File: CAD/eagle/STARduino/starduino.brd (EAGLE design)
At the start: 160 x 100 mm, 129 parts, among them J1 MICRO_SD, J2 J30J-9, J3 J30J-15, J4 J30J-31, J5 RPI-ZERO, J6 RPI-CSI, Q1 FDG8842CZ, Q2 FDG8842CZ, Q3 FDG8842CZ, Q4 FDG8842CZ, Q5 DMMT5401, Q6 DMG2305UX, T1 750313972, U1 ATSAMD21G18, U10 TCA9535_RTW_24, U11 DRV8846RGER, U12 MC14504BDTG, U13 PCA9306DCT, U14 MC74VHC1GT125DT, U15 MC74VHC1GT125DT, U16 MIC5216, U17 LT8301, U2 P82B715, U3 ADXL375BCCZ, U4 MAX31725MTA+, U5 LTC3112FE, U6 DS3231MZ+, U7 BMX055, U8 MT25QL01GBBB8ESF-0AAT, U9 LT3465/A

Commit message: more layout things, MDM adjustments
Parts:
- C1, C2: value 100nF -> 10uF; device resistor:C0603 -> resistor:C1206
- C10, C24, C25: value 1uF -> 100nF
- C11: value 10uF -> 22pF
- C12, C17: value 10uF -> 47pF
- C14: value 100nF -> 680pF
- C15, C3, C4: value 100nF -> 1uF
- C16: value 100nF -> 4.7uF; device resistor:C0603 -> CM_passives:KEMET_B
- C18: value 100nF -> 47uF; device resistor:C0603 -> resistor:C1210
- C19: value 100nF -> 10uF
- C20: value 1nF -> 10uF
- C26: value 10uF -> 1uF; device rcl:C0603 -> resistor:C0603
- C27: value 100nF -> 1uF; device rcl:C0603 -> resistor:C0603
- C28: value 2.2uF -> 1μF; device rcl:C0603 -> resistor:C0603
- C29: value 100nF -> 4.7uF; device resistor:C0603 -> resistor:A/3216-18R
- C30: value 1uF -> 10uF
- C31: value 10uF -> 100nF; device resistor:C1206 -> resistor:C0603
- C32: value 680pF -> 100nF
- C33: value 22pF -> 100nF
- C34, C35: value 47pF -> 100nF
- C36: value 47uF -> 100nF; device resistor:C1210 -> resistor:C0603
- C37: value 1uF -> 2.2uF; device resistor:C0603 -> rcl:C0603
- C38: value 4.7uF -> 10uF; device resistor:A/3216-18R -> rcl:C0603
- C39: value 10uF -> 100nF; device resistor:C1206 -> rcl:C0603
- C40: value 4.7uF -> 1uF; device CM_passives:KEMET_B -> resistor:C0603
- C41: value 1μF -> 100nF
- C5: value 1uF -> 1nF
- C6: value 6.8pF -> 100nF
- C8: value 100nF -> 6.8pF
- D1: value CMHD4448 -> CMDZ5257B; device CM_diodes:SOD123 -> CM_diodes:SOD323-W
- D2: value CMDZ5257B -> CMHD4448; device CM_diodes:SOD323-W -> CM_diodes:SOD123
- J1: value MICRO_SD -> J30J-9; device NR_connectors:MICROSD_PUSH_PUSH_AMPHENOL -> CM_J30J:ZKN-9
- J2: value J30J-9 -> MICRO_SD; device CM_J30J:ZKN-9 -> NR_connectors:MICROSD_PUSH_PUSH_AMPHENOL
- L1: value 10uH -> 22uH; device AR_passives:0603 -> AR_passives:VLF504012MT(TDK)
- L2: value 10uH -> 4.7uH; device AR_passives:0603 -> CM_passives:SRP5030
- L5: value 4.7uH -> 10uH; device CM_passives:SRP5030 -> AR_passives:0603
- L6: value 22uH -> 10uH; device AR_passives:VLF504012MT(TDK) -> AR_passives:0603
- Q3: value FDG8842CZ -> DMMT5401; device NR_Transistor:SC-70-6 -> transistor-pnp:SOT-26
- Q4: value FDG8842CZ -> DMG2305UX; device NR_Transistor:SC-70-6 -> microbuilder:SOT23-R
- Q5: value DMMT5401 -> FDG8842CZ; device transistor-pnp:SOT-26 -> NR_Transistor:SC-70-6
- Q6: value DMG2305UX -> FDG8842CZ; device microbuilder:SOT23-R -> NR_Transistor:SC-70-6
- R10: value 1.05 -> 100k; device rcl:R0603 -> resistor:R0603
- R11, R14: value 10k -> 191k; device rcl:R0603 -> resistor:R0603
- R12: value 10k -> 100k; device rcl:R0603 -> resistor:R0603
- R13: value 10k -> 4.7k; device rcl:R0603 -> resistor:R0603
- R15: value 4.7k -> 10k; device rcl:R0603 -> resistor:R0603
- R16: value 4.7k -> 47k; device rcl:R0603 -> resistor:R0603
- R17: value 220k -> 10k
- R18: value 10k -> 3.6k; device rcl:R0603 -> resistor:R0603
- R19: value 4.7k -> 6.8k
- R22: value 100k -> 10k; device resistor:R0603 -> rcl:R0603
- R23: value 191k -> 10k; device resistor:R0603 -> rcl:R0603
- R24: value 100k -> 1.05; device resistor:R0603 -> rcl:R0603
- R25: value 191k -> 1.05; device resistor:R0603 -> rcl:R0603
- R26: value 191k -> 100k
- R27: value 100k -> 4.7k
- R29: value 100k -> 4.7k; device resistor:R0603 -> rcl:R0603
- R3: value 3.6k -> 270k
- R30: value 33k -> 220k; device resistor:R0603 -> rcl:R0603
- R31: value 33k -> 10k; device resistor:R0603 -> rcl:R0603
- R32: value 158k -> 4.7k; device resistor:R0603 -> rcl:R0603
- R33: value 845k -> 4.7k
- R34: device resistor:R0603 -> rcl:R0603
- R35: value 270k -> 100k
- R36: value 47k -> 4.7k
- R37: value 10k -> 191k
- R4: value 6.8k -> 6.2
- R5, R6: value 4.7k -> 33k
- R7: value 4.7k -> 845k
- R8: value 6.2 -> 158k
- R9: value 1.05 -> 10k; device rcl:R0603 -> resistor:R0603
- U1: value ATSAMD21G18 -> LT8301; device AR_mcu:48-TQFP -> CM_IC:SOT23-5L
- U10: value TCA9535_RTW_24 -> MC74VHC1GT125DT; device MotorDriver:RTW24_2P45X2P45 -> MotorDriver:TSOP-5
- U11: value DRV8846RGER -> TCA9535_RTW_24; device MotorDriver:VQFN6 -> MotorDriver:RTW24_2P45X2P45
- U12: value MC14504BDTG -> MAX31725MTA+; device MotorDriver:TSSOP16 -> NR_IC:DFN-8
- U13: value PCA9306DCT -> BMX055; device MotorDriver:SSOP8 -> NR_IC:LGA-20
- U14: value MC74VHC1GT125DT -> DRV8846RGER; device MotorDriver:TSOP-5 -> MotorDriver:VQFN6
- U15: value MC74VHC1GT125DT -> P82B715; device MotorDriver:TSOP-5 -> CM_IC:SO8
- U16: value MIC5216 -> MC74VHC1GT125DT; device CM_IC:SOT23-5L -> MotorDriver:TSOP-5
- U17: value LT8301 -> PCA9306DCT; device CM_IC:SOT23-5L -> MotorDriver:SSOP8
- U2: value P82B715 -> LT3465/A; device CM_IC:SO8 -> AR_IC:SOT23-6
- U3: value ADXL375BCCZ -> LTC3112FE; device NR_IC:LGA-14 -> CM_IC:TSSOP20
- U4: value MAX31725MTA+ -> DS3231MZ+; device NR_IC:DFN-8 -> NR_IC:SOIC-8
- U5: value LTC3112FE -> MT25QL01GBBB8ESF-0AAT; device CM_IC:TSSOP20 -> NR_IC:SOP2-16
- U6: value DS3231MZ+ -> ATSAMD21G18; device NR_IC:SOIC-8 -> AR_mcu:48-TQFP
- U7: value BMX055 -> MIC5216; device NR_IC:LGA-20 -> CM_IC:SOT23-5L
- U8: value MT25QL01GBBB8ESF-0AAT -> ADXL375BCCZ; device NR_IC:SOP2-16 -> NR_IC:LGA-14
- U9: value LT3465/A -> MC14504BDTG; device AR_IC:SOT23-6 -> MotorDriver:TSSOP16
- moved J6 180.1 mm to (80.0, 5.08)
- moved J4 159.7 mm to (96.5, 21.6), turned to 90 degrees
- moved U11 146.0 mm to (55.9, 58.4)
- moved JP1 140.9 mm to (27.9, 3.81), turned to 180 degrees
- moved C2 127.6 mm to (27.9, 83.8)
- moved R5 125.9 mm to (19.1, 83.8)
- moved C1 123.8 mm to (27.9, 124.5)
- moved D3 121.6 mm to (35.6, 116.8)
- moved B1 121.4 mm to (41.9, 6.35), turned to 180 degrees
- moved T1 115.6 mm to (14.0, 6.99)
- moved U1 110.5 mm to (29.2, 119.4)
- moved R8 110.1 mm to (33.0, 82.5)
- moved J5 103.2 mm to (57.1, 34.3)
- moved J2 100.9 mm to (60.3, 10.2), turned to 180 degrees
- moved J3 98.0 mm to (5.08, 26.7), turned to 90 degrees
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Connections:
- net +3V3: now also C20.1, C24.1, C25.1, C29.+, C30.1, C31.1, C32.1, C33.1, C35.1, C36.1, C9.1, J2.4, L4.1, L5.1, L6.2, Q5.4, Q6.4, R13.1, R20.2, R27.2, R28.1, R33.2, R36.2, R37.1, U12.8, U13.13, U13.3, U13.7, U17.2, U4.2, U5.2, U7.5, U8.1, U8.12, U8.6, U8.7, U9.1; no longer C1.1, C11.1, C12.1, C15.1, C16.1, C17.1, C18.1, C2.1, C3.1, C38.+, C4.1, J1.4, L1.1, L2.1, L4.2, Q1.4, Q2.4, R19.2, R20.1, R23.1, R25.1, R5.2, R6.2, R7.2, U12.1, U13.2, U14.5, U3.1, U3.12, U3.6, U3.7, U4.8, U6.2, U7.13, U7.3, U7.7, U8.2
- net +5V: now also C1.1, C17.1, C18.1, C3.1, C38.1, D1.A, L1.P$1, Q1.4, Q2.4, R11.1, R18.1, R22.1, R23.1, R29.2, R30.2, R32.2, R34.2, R7.1, U1.5, U10.5, U11.18, U11.21, U11.23, U11.24, U14.15, U2.5, U3.9, U7.1, U7.3, U9.16; no longer C25.1, C26.1, C35.1, C36.1, C37.1, D2.A, L6.P$1, Q3.4, Q4.4, R12.1, R13.2, R15.2, R16.2, R17.2, R26.1, R28.1, R3.1, R33.1, U10.18, U10.21, U10.23, U10.24, U11.15, U12.16, U15.5, U16.1, U16.3, U17.5, U5.9, U9.5
- net BIAS_GND: now also C16.N; no longer C40.N
- net BIAS_V: now also C16.P; no longer C40.P
- net DEBUG_5V: now also Q2.3; no longer Q4.3
- net DEC0: now also U11.10, U14.22; no longer U10.10, U11.22
- net DEC1: now also U11.11, U14.24; no longer U10.11, U11.24
- net DIR: now also U11.12, U14.13; no longer U10.12, U11.13
- net EN_28V: now also U1.1; no longer U17.1
- net EXTERNAL_3V3: now also Q5.3; no longer Q2.3
- net EXTERNAL_KILL: now also Q5.2, Q6.2, R12.1, R26.1, R35.1, U6.22; no longer Q1.2, Q4.2, R22.1, R24.1, R29.1, U1.22
- net GND: now also C29.-, C32.2, C33.2, C35.2, C38.2, C40.2, J1.2, J1.5, J2.6, J2.G1, J2.G2, J2.G3, Q5.1, Q6.1, R10.2, R12.2, R15.2, R16.2, R17.1, R19.2, R24.1, R25.1, R26.2, R31.1, R35.2, R4.1, R5.2, R8.2, U1.2, U10.3, U11.25, U11.9, U12.4, U12.5, U12.6, U12.7, U12.9, U13.12, U13.17, U13.20, U13.4, U13.6, U14.18, U14.PPAD, U15.4, U16.3, U17.1, U2.2, U3.1, U3.10, U3.11, U3.20, U3.PAD, U6.18, U6.35, U6.42, U7.2, U8.2, U8.4, U8.5, U9.13, U9.8; no longer C11.2, C13.2, C16.2, C17.2, C38.-, C6.2, J1.6, J1.G1, J1.G2, J1.G3, J2.2, J2.5, Q3.1, Q4.1, R10.1, R11.1, R18.1, R22.2, R24.2, R27.2, R29.2, R31.2, R32.2, R36.2, R37.2, R4.2, R8.1, R9.1, U1.18, U1.35, U1.42, U1.5, U10.25, U10.9, U11.18, U11.PPAD, U12.13, U12.8, U13.1, U14.3, U15.3, U16.2, U17.2, U2.4, U3.2, U3.5, U4.4, U4.6, U4.7, U4.9, U5.1, U5.11, U5.20, U5.4, U5.PAD, U7.12, U7.17, U7.20, U7.4, U7.6, U8.10, U9.2
- net I0: now also U11.16, U14.20; no longer U10.16, U11.20
- net I1: now also U11.17, U14.21; no longer U10.17, U11.21
- net IMUDR: now also U9.3; no longer U12.3
- net IMUINT1: now also U9.5; no longer U12.5
- net IMUINT2: now also U9.7; no longer U12.7
- net IMUINT3: now also U9.9; no longer U12.9
- net IMUINT4: now also U9.11; no longer U12.11
- net IMUINT5: now also U9.14; no longer U12.14
- net IOEINT: now also U16.4, U6.30; no longer U1.30, U14.4
- net I_SENSE: now also U6.10; no longer U1.10
- net LED_CTRL: now also U2.4, U6.14; no longer U1.14, U9.4
- net LED_GND: now also R4.2, U2.3; no longer R8.2, U9.3
- net LED_V: now also C15.1, U2.1; no longer C24.1, U9.1
- net M0: now also U11.14, U14.8; no longer U10.14, U11.8
- net M1: now also U11.15, U14.9; no longer U10.15, U11.9
- net MA1: now also U14.1; no longer U11.1
- net MA2: now also U14.3; no longer U11.3
- net MB1: now also U14.6; no longer U11.6
- net MB2: now also U14.4; no longer U11.4
- net MISO: now also J2.7, U5.8, U6.8; no longer J1.7, U1.8, U8.8
- net MOSI: now also J2.3, U5.15, U6.19; no longer J1.3, U1.19, U8.15
- net N$1: now also L3.2, U6.44; no longer L1.2, U1.44
- net N$10: now also U13.19; no longer U7.19
- net N$11: now also U13.1; no longer U7.1
- net N$12: now also U13.14; no longer U7.14
- net N$13: now also U13.15; no longer U7.15
- net N$14: now also U13.10; no longer U7.10
- net N$15: now also L1.P$2, U2.6; no longer L6.P$2, U9.6
- net N$16: now also R34.1, U14.19; no longer R13.1, U11.19
- net N$17: now also Q6.5, Q6.6, R37.2; no longer Q1.5, Q1.6, R23.2
- net N$18: now also Q5.5, Q5.6, R28.2; no longer Q2.5, Q2.6, R25.2
- net N$19: now also U11.1, U9.2; no longer U10.1, U12.2
- net N$2: now also L4.2, U6.17; no longer L2.2, U1.17
- net N$20: now also R25.2, U14.5; no longer R10.2, U11.5
- net N$21: now also R24.2, U14.2; no longer R9.2, U11.2
- net N$22: now also U10.4, U14.12; no longer U11.12, U15.4
- net N$23: now also U11.2, U9.4; no longer U10.2, U12.4
- net N$24: now also R17.2, U10.1; no longer R11.2, U15.1
- net N$25: now also U11.22, U16.2; no longer U10.22, U14.2
- net N$26: now also C37.1, U14.14, U14.17; no longer C28.1, U11.14, U11.17
- net N$27: now also R31.2, U16.1; no longer R18.2, U14.1
- net N$28: now also U11.3, U9.6; no longer U10.3, U12.6
- net N$29: now also U11.4, U9.10; no longer U10.4, U12.10
- net N$3: now also L5.2, U6.36; no longer L3.2, U1.36
- net N$30: now also U11.5, U9.12; no longer U10.5, U12.12
- net N$31: now also U11.6, U9.15; no longer U10.6, U12.15
- net N$32: now also R13.2, U5.1, U5.3; no longer R20.2, U8.1, U8.3
- net N$33: now also R32.1, U11.20, U17.8; no longer R16.1, U10.20, U13.8
- net N$34: now also R29.1, U11.19, U17.7; no longer R15.1, U10.19, U13.7
- net N$35: now also R30.1, U17.5, U17.6; no longer R17.1, U13.5, U13.6
- net N$36: now also C40.1, C41.1, Q6.3, U15.8; no longer C10.1, C13.1, Q1.3, U2.8
- net N$37: now also Q1.5, Q1.6, R11.2; no longer Q3.5, Q3.6, R26.2
- net N$38: now also Q2.5, Q2.6, R14.2; no longer Q4.5, Q4.6, R28.2
- net N$39: now also C6.1, L2.P$1, U3.15, U3.16; no longer C14.1, L5.P$1, U5.15, U5.16
- net N$4: now also U6.6; no longer U1.6
- net N$40: now also C13.1, L2.P$2, U3.12, U3.13; no longer C29.1, L5.P$2, U5.12, U5.13
- net N$41: now also C6.2, U3.17; no longer C14.2, U5.17
- net N$42: now also C13.2, U3.14; no longer C29.2, U5.14
- net N$43: now also C4.1, U3.18; no longer C30.1, U5.18
- net N$44: now also C11.1, C14.1, U3.2; no longer C32.1, C33.1, U5.2
- net N$45: now also C11.2, R6.2, R7.2, R8.1, R9.1, U3.3; no longer C33.2, R30.2, R32.1, R33.2, R34.1, U5.3
- net N$46: now also C14.2, R6.1; no longer C32.2, R30.1
- net N$47: now also C12.1, R5.1, U3.8; no longer C34.1, R31.1, U5.8
- net N$48: now also C17.2, R9.2; no longer C35.2, R34.2
- net N$49: now also R3.2, U1.3; no longer R35.2, U17.3
- net N$5: now also C26.1, U6.43; no longer C5.1, U1.43
- net N$50: now also D2.A, R3.1, U1.4; no longer D1.A, R35.1, U17.4
- net N$53: now also Q3.5, Q4.3; no longer Q5.5, Q6.3
- net N$54: now also Q3.4, Q4.1, R16.1; no longer Q5.4, Q6.1, R36.1
- net N$55: now also Q3.1, Q3.2, Q3.3, R15.1; no longer Q5.1, Q5.2, Q5.3, R37.1
- net N$56: now also C28.1, Q3.6, Q4.2; no longer C41.1, Q5.6, Q6.2
- net N$6: now also R27.1, U12.3; no longer R7.1, U4.3
- net N$8: now also C5.1, U4.6; no longer C20.1, U6.6
- net N$9: now also U13.2; no longer U7.2
- net NENBL: now also R23.2, U11.8, U14.11; no longer R14.2, U10.8, U11.11
- net NFAULT: now also R22.2, U11.13, U14.7; no longer R12.2, U10.13, U11.7
- net NSLEEP: now also U11.7, U14.23; no longer U10.7, U11.23
- net PA27: now also U4.3, U6.39; no longer U1.39, U6.3
- net PB02: now also U6.47, U8.8; no longer U1.47, U3.8
- net PB03: now also U6.48, U8.9; no longer U1.48, U3.9
- net PB22: now also J2.2, U6.37; no longer J1.2, U1.37
- net PB23: now also U5.7, U6.38; no longer U1.38, U8.7
- net PI_5V: now also Q1.3; no longer Q3.3
- net PI_KILL: now also Q1.2, R10.1, U6.29; no longer Q3.2, R27.1, U1.29
- net PRESSURE_IN: now also U6.11; no longer U1.11
- net PWM/SYNC: now also U3.19; no longer U5.19
- net RESET: now also C10.1, U6.40; no longer C8.1, U1.40
- net RX0: now also J1.6, U6.16; no longer J2.6, U1.16
- net RX1: now also U6.28; no longer U1.28
- net RX2: now also U6.12; no longer U1.12
- net SCK: now also J2.5, U5.16, U6.20; no longer J1.5, U1.20, U8.16
- net SCL: now also R21.1, U12.2, U13.9, U15.3, U17.3, U4.8, U6.32, U8.14; no longer R6.1, U1.32, U13.3, U2.3, U3.14, U4.2, U6.8, U7.9
- net SCL_BUFF: now also R36.1, U15.2; no longer R21.1, U2.2
- net SDA: now also R20.1, U12.1, U13.11, U15.6, U17.4, U4.7, U6.31, U8.13; no longer R5.1, U1.31, U13.4, U2.6, U3.13, U4.1, U6.7, U7.11
- net SDA_BUFF: now also R33.1, U15.7; no longer R19.1, U2.7
- net STEPFREQ: now also U10.2, U6.7; no longer U1.7, U15.2
- net SWDCLK: now also U6.45; no longer U1.45
- net SWDIO: now also U6.46; no longer U1.46
- net SYNC: now also U6.21; no longer U1.21
- net TX0: now also J1.7, U6.15; no longer J2.7, U1.15
- net TX1: now also U6.27; no longer U1.27
- net TX2: now also U6.9; no longer U1.9
- net USB_D+: now also U6.34; no longer U1.34
- net USB_D-: now also U6.33; no longer U1.33
- net VCC: now also C2.1, J1.1, U3.5, U3.6, U3.7; no longer C31.1, J2.1, U5.5, U5.6, U5.7
- net VREFA: now also C34.1, L6.1, U6.4; no longer C9.1, L4.1, U1.4
- net V_SENSE: now also R18.2, R19.1, U6.3; no longer R3.2, R4.1, U1.3
- net XIN32: now also C7.1, U6.1; no longer C6.1, U1.1
- net XOUT32: now also C8.1, U6.2; no longer C7.1, U1.2
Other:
- board size 160 x 100 mm -> 101.6 x 38.1 mm

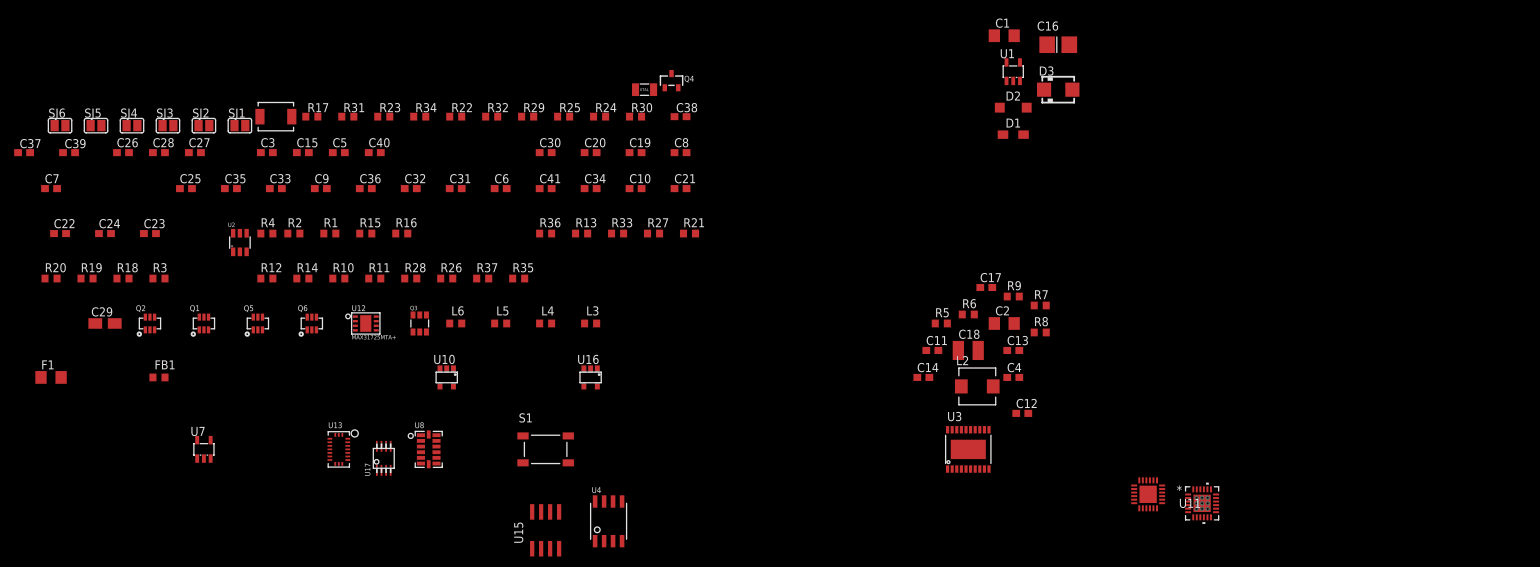
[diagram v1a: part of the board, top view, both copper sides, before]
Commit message: Cleaned up some symbols
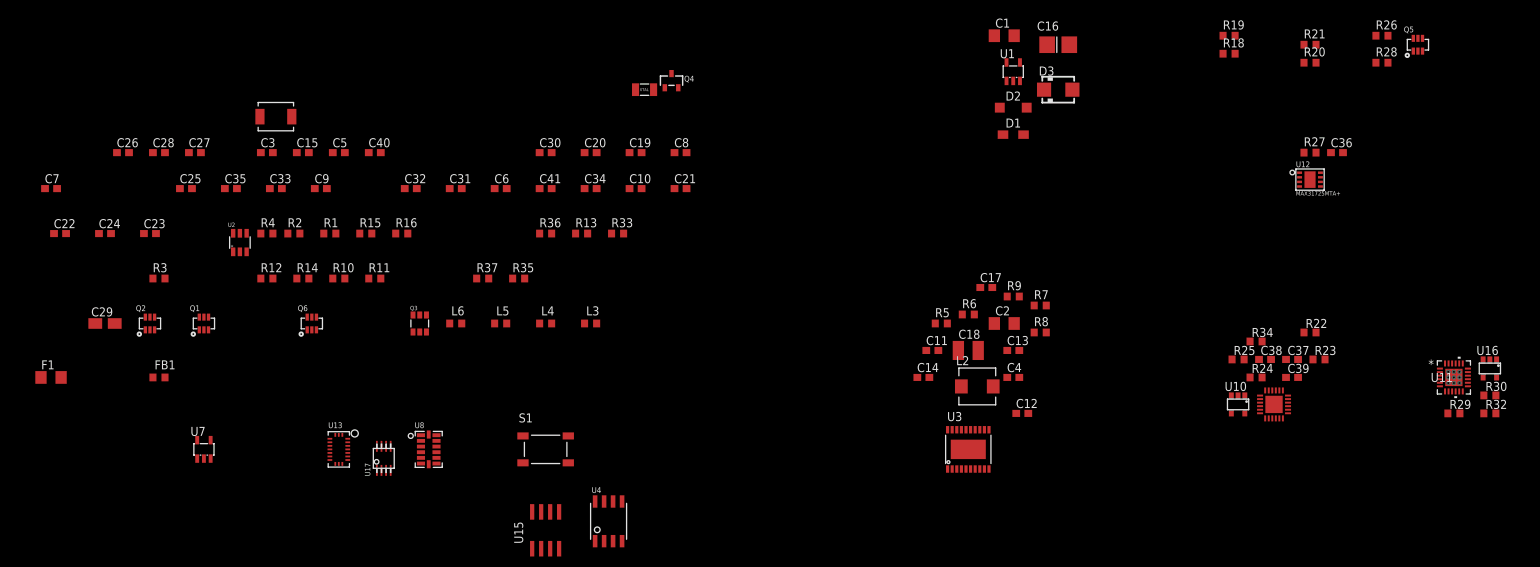
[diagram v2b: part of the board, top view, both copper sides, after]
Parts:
- removed R17, R31: 10k, rcl:R0603
- removed SJ1, SJ2, SJ3, SJ4, SJ5, SJ6: (no value), jumper:SJ
- moved C37 181.4 mm to (68.6, 78.7)
- moved R20 180.4 mm to (71.1, 120.7)
- moved C39 175.6 mm to (68.6, 76.2)
- moved Q5 168.5 mm to (86.4, 123.2)
- moved R19 164.9 mm to (59.7, 124.5)
- moved R18 159.4 mm to (59.7, 121.9)
- moved R32 147.1 mm to (96.5, 71.1)
- moved R28 140.5 mm to (81.3, 120.7)
- moved R29 137.4 mm to (91.4, 71.1)
- moved C36 137.3 mm to (74.9, 108.0)
- moved R23 136.5 mm to (72.4, 78.7)
- moved R26 136.5 mm to (81.3, 124.5)
- moved U12 134.9 mm to (71.1, 104.1)
- moved U16 127.0 mm to (96.5, 77.5)
- moved R30 126.9 mm to (96.5, 73.7)
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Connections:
- removed net N$10: SJ2.1, U13.19
- removed net N$11: SJ3.1, U13.1
- removed net N$12: SJ4.1, U13.14
- removed net N$13: SJ5.1, U13.15
- removed net N$14: SJ6.1, U13.10
- removed net N$24: R17.2, U10.1
- removed net N$27: R31.2, U16.1
- removed net N$9: SJ1.1, U13.2
- net GND: now also U10.1, U16.1; no longer R17.1, R31.1
- net IMUDR: now also U13.2; no longer SJ1.2
- net IMUINT1: now also U13.19; no longer SJ2.2
- net IMUINT2: now also U13.1; no longer SJ3.2
- net IMUINT3: now also U13.14; no longer SJ4.2
- net IMUINT4: now also U13.15; no longer SJ5.2
- net IMUINT5: now also U13.10; no longer SJ6.2

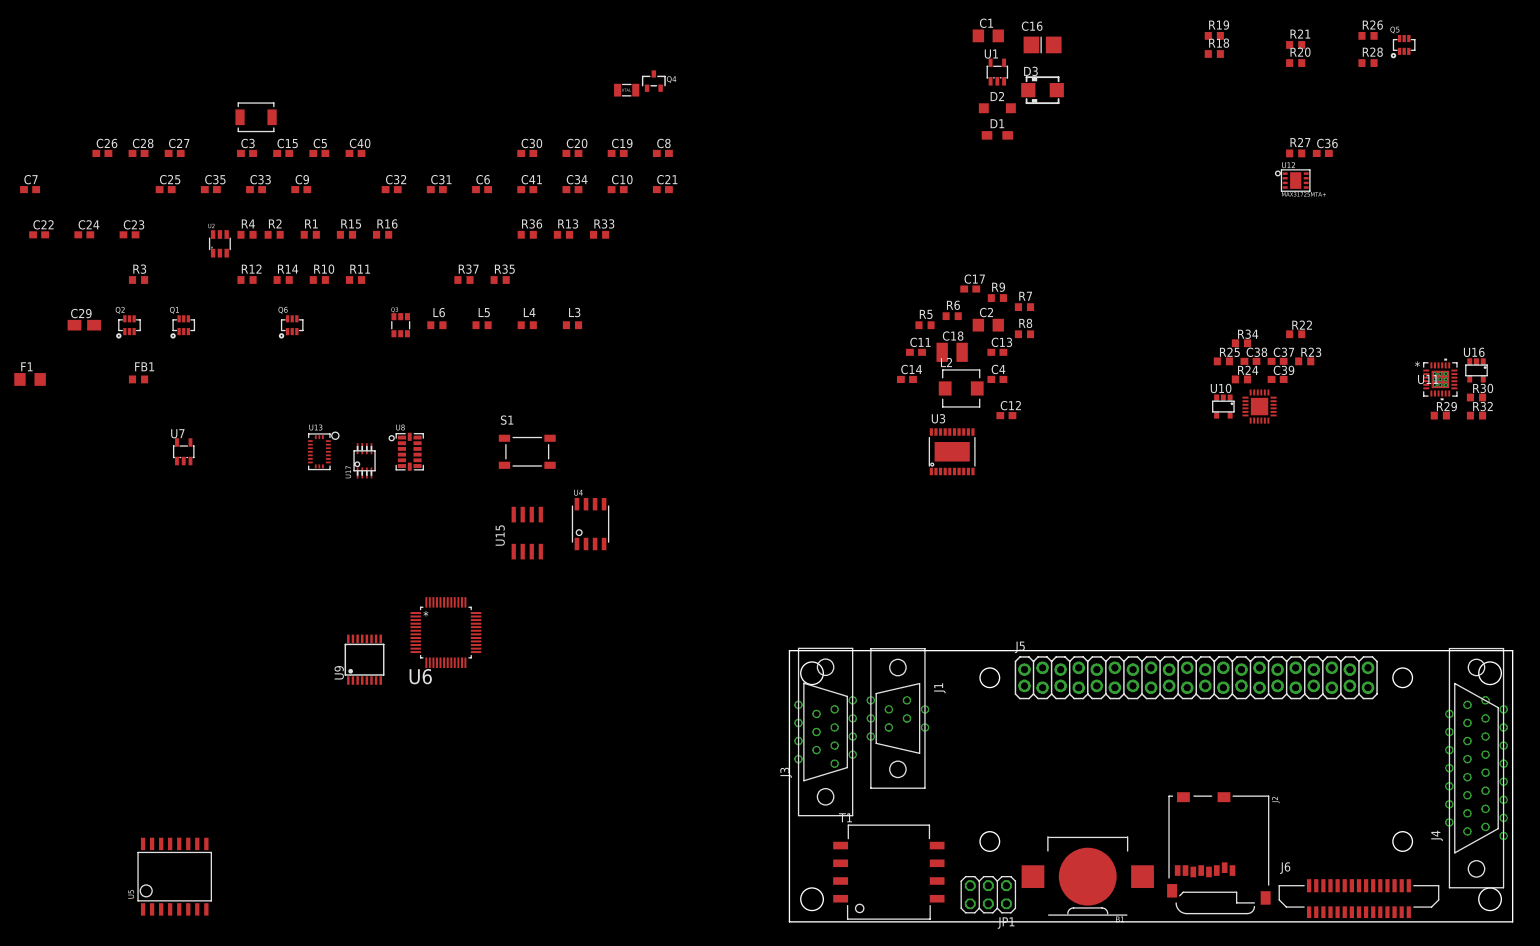
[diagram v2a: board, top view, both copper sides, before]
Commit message: Schematic updates
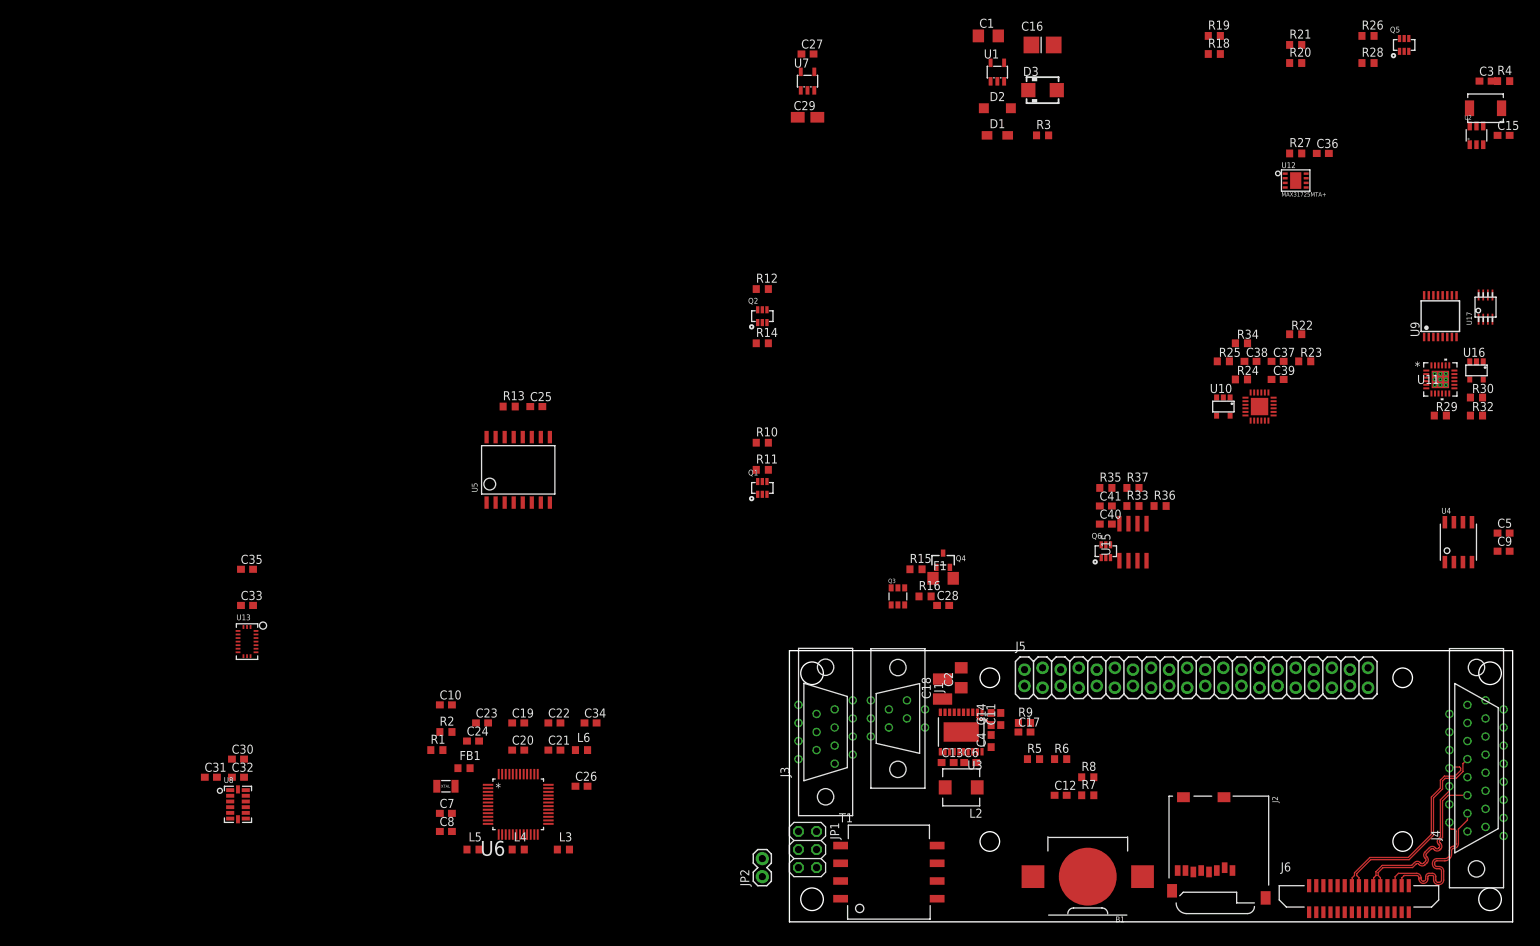
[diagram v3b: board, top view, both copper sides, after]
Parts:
- removed S1: PTS525-SM15, AR_switches:PTS525
- added JP2: (no value), CM_passives:1X02
- moved R4 177.8 mm to (100.3, 118.1)
- moved U2 177.2 mm to (96.5, 110.5)
- moved C9 176.4 mm to (100.3, 52.1)
- moved C5 174.7 mm to (100.3, 54.6)
- moved C3 174.3 mm to (97.8, 118.1)
- moved L1 172.7 mm to (97.8, 114.3)
- moved C15 171.5 mm to (100.3, 110.5)
- moved U17 159.0 mm to (97.8, 86.4)
- moved U9 158.6 mm to (91.4, 85.1)
- moved F1 131.3 mm to (21.6, 48.3)
- moved C28 129.6 mm to (21.6, 44.5)
- moved R3 128.6 mm to (35.6, 110.5)
- moved U4 121.9 mm to (94.0, 53.3)
- moved Q6 118.6 mm to (44.5, 52.1)
- moved C40 117.6 mm to (44.5, 55.9)
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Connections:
- net CAM1_DN1 renamed CAM1_D1_N
- net CAM1_DP1 renamed CAM1_D1_P
- net N$44 renamed COMP_5
- net N$45 renamed FB_5
- removed net CAM1_CN: J4.24, J6.8
- removed net CAM1_CP: J4.25, J6.9
- removed net CAM1_DN0: J4.18, J6.2
- removed net CAM1_DP0: J4.19, J6.3
- removed net N$47: C12.1, R5.1, U3.8
- new net CAM1_C_N: J4.25, J6.8
- new net CAM1_C_P: J4.24, J6.9
- new net CAM1_D0_N: J4.19, J6.2
- new net CAM1_D0_P: J4.18, J6.3
- net GND: now also J1.3, J1.4, JP2.1; no longer J1.2, S1.1, S1.2
- net I_SENSE: now also C12.1, R5.1, U3.8
- net N$7: now also JP2.2; no longer S1.3, S1.4
- net PWM/SYNC: now also U6.23
- net SYNC: now also J5.37
- net VCC: now also J1.2
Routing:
- net CAM1_C_P: track 0.00 -> 28.6 mm
- net CAM1_C_N: track 0.00 -> 28.4 mm
- net CAM1_D1_N: track 0.00 -> 24.0 mm
- net CAM1_D1_P: track 0.00 -> 22.7 mm
- net CAM1_D0_N: track 0.00 -> 22.5 mm
- net CAM1_D0_P: track 0.00 -> 21.6 mm
- net COMP_5: track 0.00 -> 3.12 mm

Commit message: Layout and schematic progress
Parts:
- added TP1, TP2: TESTPOINT, CM_passives:TP-2MM
- J1: value J30J-9 -> J30J-9J30; device CM_J30J:ZKN-9 -> CM_J30J:ZKN-9-J30
- J3: value J30J-15 -> J30J-15J30; device CM_J30J:ZKN-15 -> CM_J30J:ZKN-15-J30
- J4: value J30J-31 -> J30J-31J30; device CM_J30J:ZKN-31 -> CM_J30J:ZKN-31-J30
- moved C1 121.8 mm to (25.6, 2.70), turned to 270 degrees
- moved U1 116.8 mm to (28.2, 2.54)
- moved R4 112.9 mm to (73.2, 8.49), turned to 270 degrees
- moved C16 109.9 mm to (12.1, 15.8), turned to 180 degrees
- moved C3 109.2 mm to (74.7, 11.4), turned to 270 degrees
- moved D2 108.0 mm to (25.4, 6.35)
- moved D1 107.8 mm to (23.3, 2.86), turned to 270 degrees
- moved C15 107.8 mm to (68.5, 7.54), turned to 90 degrees
- moved U2 105.8 mm to (70.9, 7.86)
- moved L1 105.6 mm to (70.8, 12.2), turned to 180 degrees
- moved R3 104.6 mm to (29.0, 6.11), turned to 90 degrees
- moved D3 102.4 mm to (18.2, 16.0)
- moved JP2 98.8 mm to (91.1, 33.7)
- moved C9 74.9 mm to (34.3, 16.7), turned to 90 degrees
- moved C39 74.5 mm to (121.9, 24.1)
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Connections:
- removed net C_GND: J4.17, J4.20, J4.23, J4.26, J6.1, J6.10, J6.4, J6.7
- removed net PI_D+: J3.7
- removed net PI_D1: J3.8
- new net PI_D_N: J3.8, TP2.P$1
- new net PI_D_P: J3.7, TP1.P$1
- new net USB_D_N: J3.4
- new net USB_D_P: J3.3
- net BIAS_GND: now also J4.3; no longer J4.4
- net BIAS_V: now also J4.4; no longer J4.3
- net CAM1_C_N: now also J4.24; no longer J4.25
- net CAM1_C_P: now also J4.25; no longer J4.24
- net CAM1_D0_N: now also J4.18; no longer J4.19
- net CAM1_D0_P: now also J4.19; no longer J4.18
- net GND: now also J4.17, J4.20, J4.23, J4.26, J6.1, J6.10, J6.4, J6.7
- net USB_D+: no longer J3.3
- net USB_D-: no longer J3.4
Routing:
- net BIAS_GND: track 0.00 -> 109.2 mm, vias 0 -> 2
- net BIAS_V: track 0.00 -> 104.5 mm, vias 0 -> 2
- net LED_V: track 0.00 -> 37.7 mm, vias 0 -> 1
- net LED_GND: track 0.00 -> 34.5 mm, vias 0 -> 1
- net C_3V3: track 0.00 -> 33.8 mm
- net C_SDA0: track 0.00 -> 33.4 mm
- net C_SCL0: track 0.00 -> 30.4 mm
- net CAM_CLK: track 0.00 -> 30.1 mm
- net CAM_GPIO: track 0.00 -> 27.5 mm
- net GND: track 0.00 -> 15.5 mm, vias 0 -> 2
- net I_SENSE: track 0.00 -> 14.4 mm, vias 0 -> 2
- net FB_5: track 0.00 -> 13.6 mm
- net N$52: track 0.00 -> 6.76 mm
- net N$49: track 0.00 -> 6.51 mm
- net PWM/SYNC: track 0.00 -> 6.38 mm
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- added copper zone on layer 1, net +5V
- added copper zone on layer 1, net GND
- added copper zone on layer 16, net GND
- added copper zone on layer 1, net LED_GND
- added copper zone on layer 1, net LED_V
- added copper zone on layer 1, net N$15
- added copper zone on layer 1, net N$39
- added copper zone on layer 1, net N$40
- added copper zone on layer 1, net N$50
- added copper zone on layer 1, net N$51
- added copper zone on layer 1, net VCC
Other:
- outline, holes or cut-outs redrawn
